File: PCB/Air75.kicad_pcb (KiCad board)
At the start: 2 copper layers, 78.7 x 58.4 mm, 22 parts, among them J1 OLED_128x32, SW1 SW_Push_45deg, SW12 RotaryEncoder_Switch, SW2 SW_Push_45deg, SW3 SW_Push_45deg, SW4 SW_Push_45deg, SW5 SW_Push_45deg, SW6 SW_Push_45deg, SW7 SW_Push_45deg, SW8 SW_Push_45deg, SW9 SW_Push_45deg, U1 XIAO-RP2040-DIP

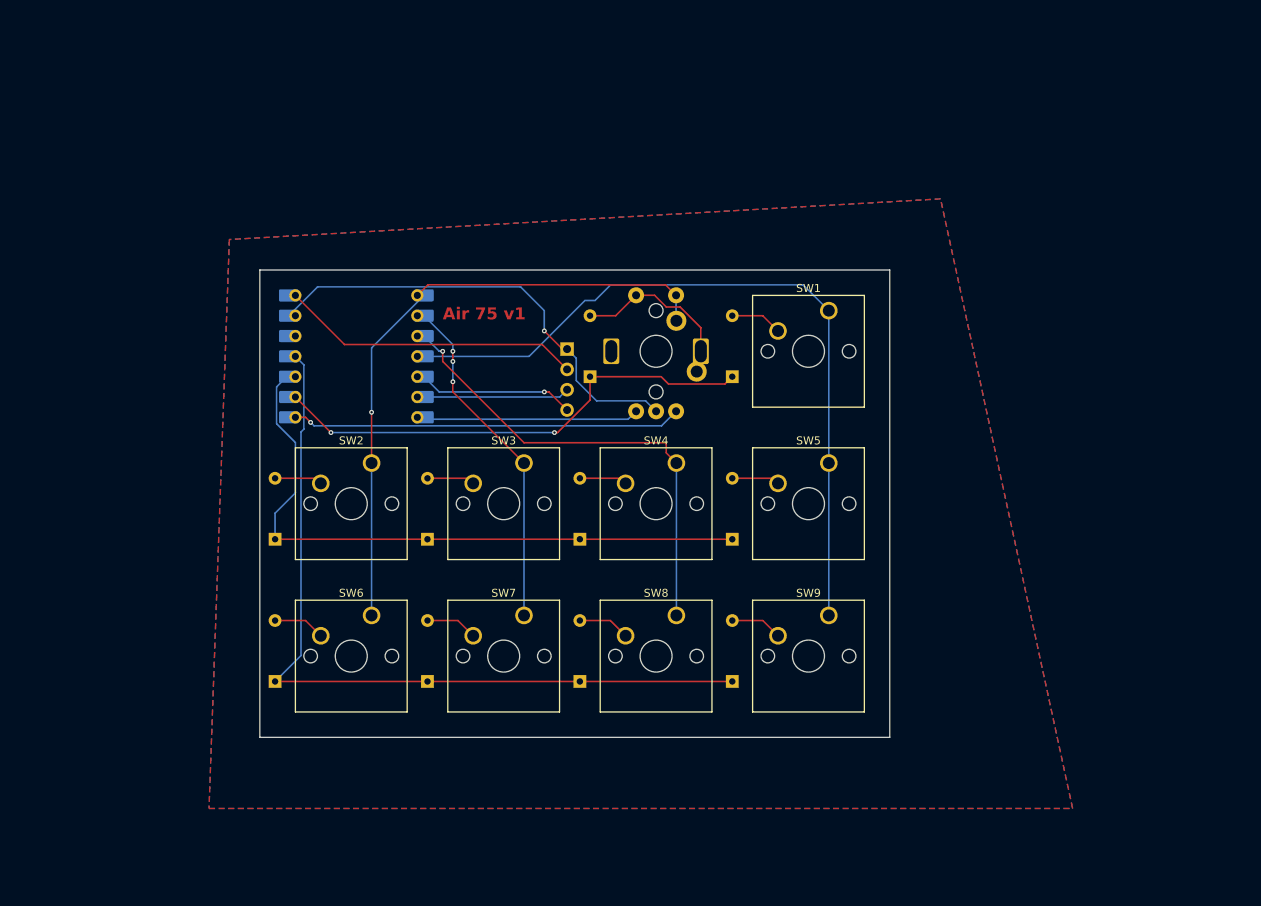
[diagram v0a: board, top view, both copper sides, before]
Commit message: fix: remove right angles from pcb
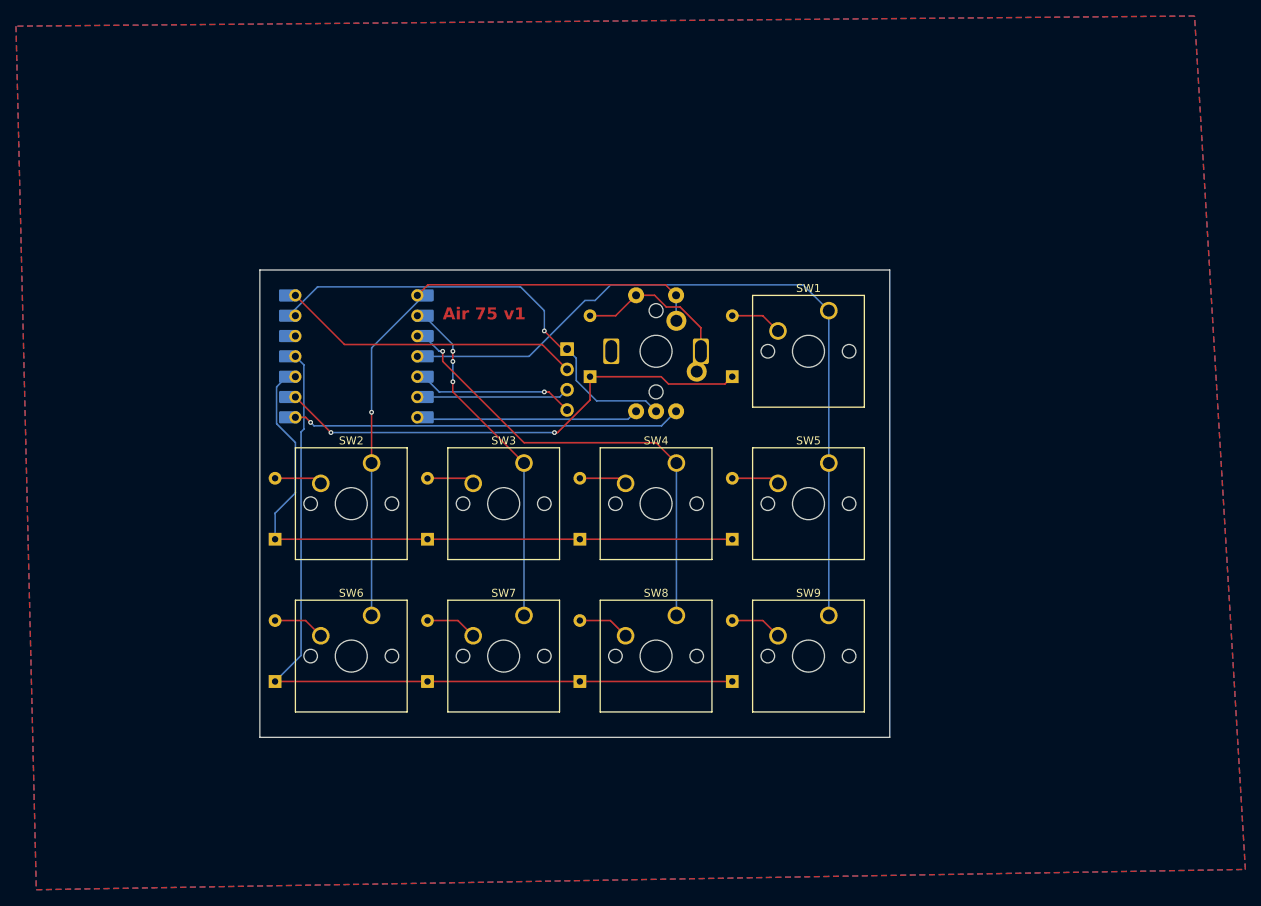
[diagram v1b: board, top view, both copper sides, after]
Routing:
- net Column 2: track 58.7 -> 57.9 mm
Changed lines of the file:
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@@
+	)
+	(segment
+		(start 133.35 83.82)
+		(end 149.86 83.82)
+		(width 0.2)
+		(layer "F.Cu")
+		(net 20)
 	)
 	(segment
@@
 	)
 	(segment
-		(start 133.35 83.82)
-		(end 151.13 83.82)
+		(start 149.86 83.82)
+		(end 152.4 86.36)
 		(width 0.2)
 		(layer "F.Cu")
@@
 		(start 123.19 73.66)
 		(end 133.35 83.82)
-		(width 0.2)
-		(layer "F.Cu")
-		(net 20)
-	)
-	(segment
-		(start 151.13 83.82)
-		(end 151.13 85.09)
-		(width 0.2)
-		(layer "F.Cu")
-		(net 20)
-	)
-	(segment
-		(start 151.13 85.09)
-		(end 152.4 86.36)
 		(width 0.2)
 		(layer "F.Cu")
@@
 		(polygon
 			(pts
-				(xy 96.52 58.42) (xy 93.98 129.54) (xy 201.93 129.54) (xy 185.42 53.34)
+				(xy 69.85 31.75) (xy 72.39 139.7) (xy 223.52 137.16) (xy 217.17 30.48)
 			)
 		)

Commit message: fix: fix pcb
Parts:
- moved J1 4.05 mm to (140.0, 77.9)
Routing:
- net Disp SCL: track 18.7 -> 21.6 mm
- net +5V: track 37.8 -> 36.6 mm
- net GND: track 57.0 -> 57.7 mm
- net Disp SDA: track 19.6 -> 19.1 mm
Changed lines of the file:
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@@
 			)
 		)
+		(model "${SCOTTOKEEBS_KICAD}/3dmodels/ScottoKeebs_MX.3dshapes/MX_PCB.step"
+			(offset
+				(xyz -2.6 -5.1 0)
+			)
+			(scale
+				(xyz 1 1 1)
+			)
+			(rotate
+				(xyz 0 0 0)
+			)
+		)
 	)
 	(footprint "ScottoKeebs_Scotto:Encoder_EC11_MX_Combo"
@@
 			)
 			(rotate
-				(xyz -90 0 90)
+				(xyz -90 0 -90)
+			)
+		)
+		(model "${SCOTTO_KICAD}/3dmodels/ScottoKeebs_Scotto.3dshapes/EC11.step"
+			(hide yes)
+			(offset
+				(xyz 0 0 0)
+			)
+			(scale
+				(xyz 1 1 1)
+			)
+			(rotate
+				(xyz -90 0 -90)
 			)
 		)
@@
 			)
 		)
+		(model "${SCOTTOKEEBS_KICAD}/3dmodels/ScottoKeebs_MX.3dshapes/MX_PCB.step"
+			(offset
+				(xyz -2.6 -5.1 0)
+			)
+			(scale
+				(xyz 1 1 1)
+			)
+			(rotate
+				(xyz 0 0 0)
+			)
+		)
 	)
 	(footprint "Button_Switch_Keyboard:SW_Cherry_MX_1.00u_PCB"
@@
 			)
 		)
+		(model "${SCOTTOKEEBS_KICAD}/3dmodels/ScottoKeebs_MX.3dshapes/MX_PCB.step"
+			(offset
+				(xyz -2.6 -5.1 0)
+			)
+			(scale
+				(xyz 1 1 1)
+			)
+			(rotate
+				(xyz 0 0 0)
+			)
+		)
 	)
 	(footprint "Button_Switch_Keyboard:SW_Cherry_MX_1.00u_PCB"
@@
 			)
 		)
+		(model "${SCOTTO_KICAD}/3dmodels/ScottoKeebs_MX.3dshapes/MX_PCB.step"
+			(offset
+				(xyz -2.6 -5.1 0)
+			)
+			(scale
+				(xyz 1 1 1)
+			)
+			(rotate
+				(xyz 0 0 0)
+			)
+		)
 	)
 	(footprint "Button_Switch_Keyboard:SW_Cherry_MX_1.00u_PCB"
@@
 			)
 		)
+		(model "${SCOTTOKEEBS_KICAD}/3dmodels/ScottoKeebs_MX.3dshapes/MX_PCB.step"
+			(offset
+				(xyz -2.6 -5.1 0)
+			)
+			(scale
+				(xyz 1 1 1)
+			)
+			(rotate
+				(xyz 0 0 0)
+			)
+		)
 	)
 	(footprint "ScottoKeebs_Components:OLED_128x32"
 		(layer "F.Cu")
-		(at 140.335 81.915 180)
+		(at 140.03 77.872 180)
 		(property "Reference" "J1"
 			(at 7.75 10 0)
@@
 			)
 		)
+		(model "${SCOTTO_KICAD}/3dmodels/ScottoKeebs_Components.3dshapes/OLED_128x32.step"
+			(offset
+				(xyz 19.25 -6 0)
+			)
+			(scale
+				(xyz 1 1 1)
+			)
+			(rotate
+				(xyz 0 0 0)
+			)
+		)
 	)
 	(footprint "Button_Switch_Keyboard:SW_Cherry_MX_1.00u_PCB"
@@
 			)
 		)
+		(model "${SCOTTOKEEBS_KICAD}/3dmodels/ScottoKeebs_MX.3dshapes/MX_PCB.step"
+			(offset
+				(xyz -2.6 -5.1 0)
+			)
+			(scale
+				(xyz 1 1 1)
+			)
+			(rotate
+				(xyz 0 0 0)
+			)
+		)
 	)
 	(footprint "Button_Switch_Keyboard:SW_Cherry_MX_1.00u_PCB"
@@
 			)
 		)
+		(model "${SCOTTOKEEBS_KICAD}/3dmodels/ScottoKeebs_MX.3dshapes/MX_PCB.step"
+			(offset
+				(xyz -2.6 -5.1 0)
+			)
+			(scale
+				(xyz 1 1 1)
+			)
+			(rotate
+				(xyz 0 0 0)
+			)
+		)
 	)
 	(footprint "Button_Switch_Keyboard:SW_Cherry_MX_1.00u_PCB"
@@
 			)
 		)
+		(model "${SCOTTOKEEBS_KICAD}/3dmodels/ScottoKeebs_MX.3dshapes/MX_PCB.step"
+			(offset
+				(xyz -2.6 -5.1 0)
+			)
+			(scale
+				(xyz 1 1 1)
+			)
+			(rotate
+				(xyz 0 0 0)
+			)
+		)
 	)
 	(footprint "Button_Switch_Keyboard:SW_Cherry_MX_1.00u_PCB"
@@
 			)
 		)
+		(model "${SCOTTOKEEBS_KICAD}/3dmodels/ScottoKeebs_MX.3dshapes/MX_PCB.step"
+			(offset
+				(xyz -2.6 -5.1 0)
+			)
+			(scale
+				(xyz 1 1 1)
+			)
+			(rotate
+				(xyz 0 0 0)
+			)
+		)
 	)
 	(footprint "Diode_THT:D_DO-35_SOD27_P7.62mm_Horizontal"
@@
 			)
 		)
+		(model "C:/krish/KiCad/xiao.step"
+			(offset
+				(xyz 0 0 0)
+			)
+			(scale
+				(xyz 1 1 1)
+			)
+			(rotate
+				(xyz 0 0 0)
+			)
+		)
 	)
 	(footprint "Diode_THT:D_DO-35_SOD27_P7.62mm_Horizontal"
@@
 	)
 	(segment
-		(start 135.89 77.47)
-		(end 136.47 77.47)
+		(start 136.47 77.47)
+		(end 138.248 75.692)
 		(width 0.2)
 		(layer "F.Cu")
@@
 	)
 	(segment
-		(start 136.47 77.47)
-		(end 138.735 79.735)
+		(start 138.248 75.692)
+		(end 138.43 75.692)
+		(width 0.2)
+		(layer "F.Cu")
+		(net 14)
+	)
+	(segment
+		(start 135.89 77.47)
+		(end 136.47 77.47)
 		(width 0.2)
 		(layer "F.Cu")
@@
 	)
 	(segment
-		(start 138.735 77.195)
-		(end 138.705 77.195)
+		(start 137.16 74.422)
+		(end 138.43 73.152)
 		(width 0.2)
-		(layer "F.Cu")
+		(layer "B.Cu")
 		(net 15)
 	)
 	(segment
-		(start 138.705 77.195)
-		(end 138.43 77.47)
+		(start 137.16 77.724)
+		(end 137.16 74.422)
 		(width 0.2)
-		(layer "F.Cu")
+		(layer "B.Cu")
 		(net 15)
 	)
 	(segment
-		(start 137.825 78.105)
-		(end 138.735 77.195)
+		(start 120.85 78.105)
+		(end 136.779 78.105)
 		(width 0.2)
 		(layer "B.Cu")
@@
 	)
 	(segment
-		(start 120.85 78.105)
-		(end 137.825 78.105)
+		(start 136.779 78.105)
+		(end 137.16 77.724)
 		(width 0.2)
 		(layer "B.Cu")
@@
 	)
 	(segment
-		(start 135.89 69.85)
-		(end 138.155 72.115)
+		(start 136.652 68.072)
+		(end 138.43 68.072)
 		(width 0.2)
 		(layer "F.Cu")
@@
 	)
 	(segment
-		(start 138.155 72.115)
-		(end 138.735 72.115)
+		(start 135.128 66.548)
+		(end 136.652 68.072)
 		(width 0.2)
 		(layer "F.Cu")
@@
 	)
 	(via
-		(at 135.89 69.85)
+		(at 135.128 66.548)
 		(size 0.6)
 		(drill 0.3)
@@
 	)
 	(segment
-		(start 148.56 78.59)
-		(end 149.86 79.89)
+		(start 139.885 76.045)
+		(end 139.885 69.527)
 		(width 0.2)
 		(layer "B.Cu")
@@
 	)
 	(segment
-		(start 107.542 64.343)
-		(end 132.923 64.343)
+		(start 142.43 78.59)
+		(end 139.885 76.045)
 		(width 0.2)
 		(layer "B.Cu")
@@
 	)
 	(segment
-		(start 139.885 73.265)
-		(end 139.885 76.045)
+		(start 148.56 78.59)
+		(end 142.43 78.59)
 		(width 0.2)
 		(layer "B.Cu")
@@
 	)
 	(segment
-		(start 142.43 78.59)
-		(end 148.56 78.59)
+		(start 139.885 69.527)
+		(end 138.43 68.072)
 		(width 0.2)
 		(layer "B.Cu")
@@
 	)
 	(segment
-		(start 132.923 64.343)
-		(end 135.89 67.31)
+		(start 107.542 64.343)
+		(end 132.923 64.343)
 		(width 0.2)
 		(layer "B.Cu")
@@
 	)
 	(segment
-		(start 139.885 76.045)
-		(end 142.43 78.59)
+		(start 149.86 79.89)
+		(end 148.56 78.59)
 		(width 0.2)
 		(layer "B.Cu")
@@
 	)
 	(segment
-		(start 135.89 67.31)
-		(end 135.89 69.85)
+		(start 103.94 67.945)
+		(end 107.542 64.343)
 		(width 0.2)
 		(layer "B.Cu")
@@
 	)
 	(segment
-		(start 138.735 72.115)
-		(end 139.885 73.265)
+		(start 138.372314 68.072)
+		(end 138.401157 68.043157)
 		(width 0.2)
 		(layer "B.Cu")
@@
 	)
 	(segment
-		(start 103.94 67.945)
-		(end 107.542 64.343)
+		(start 132.923 64.343)
+		(end 135.128 66.548)
 		(width 0.2)
 		(layer "B.Cu")
@@
 	)
 	(segment
-		(start 110.917 71.547)
-		(end 104.775 65.405)
+		(start 104.775 65.405)
+		(end 110.917 71.547)
 		(width 0.2)
 		(layer "F.Cu")
@@
 	)
 	(segment
-		(start 138.735 74.655)
-		(end 135.627 71.547)
+		(start 110.917 71.547)
+		(end 137.495 71.547)
 		(width 0.2)
 		(layer "F.Cu")
@@
 	)
 	(segment
-		(start 135.627 71.547)
-		(end 110.917 71.547)
+		(start 137.495 71.547)
+		(end 138.43 70.612)
 		(width 0.2)
 		(layer "F.Cu")
@@
 	)
 	(segment
-		(start 140.97 66.04)
-		(end 142.24 66.04)
+		(start 144.19 64.09)
+		(end 168.23 64.09)
 		(width 0.2)
 		(layer "B.Cu")
@@
 	)
 	(segment
-		(start 144.19 64.09)
-		(end 168.23 64.09)
+		(start 137.287 66.04)
+		(end 142.24 66.04)
 		(width 0.2)
 		(layer "B.Cu")
@@
 	)
 	(segment
-		(start 142.24 66.04)
-		(end 144.19 64.09)
+		(start 168.23 64.09)
+		(end 171.45 67.31)
 		(width 0.2)
 		(layer "B.Cu")
@@
 	)
 	(segment
-		(start 120.85 73.025)
-		(end 133.985 73.025)
+		(start 130.302 73.025)
+		(end 137.287 66.04)
 		(width 0.2)
 		(layer "B.Cu")
@@
 	)
 	(segment
-		(start 168.23 64.09)
-		(end 171.45 67.31)
+		(start 120.85 73.025)
+		(end 130.302 73.025)
 		(width 0.2)
 		(layer "B.Cu")
@@
 	)
 	(segment
-		(start 133.985 73.025)
-		(end 140.97 66.04)
+		(start 142.24 66.04)
+		(end 144.19 64.09)
 		(width 0.2)
 		(layer "B.Cu")
